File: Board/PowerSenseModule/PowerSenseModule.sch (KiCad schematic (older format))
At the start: 24 parts, among them J1 Conn_01x06_Male, U1 TPS82150

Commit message: Cleaned up main page of the schematic
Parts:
- added F?: Fuse, symbol Device:Fuse
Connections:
- net labels added: CANH, CANL, LIVE_IN, MEAS_IN, MEAS_OUT
- wire segments 101 -> 96
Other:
- note added: "MEAS_IN needs to be physically placed after caps\n"
- moved on the sheet: C1, C19, C2, C20, C21, C22, C23, C3, C4, C5, C6, C7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

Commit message: PCB update
- Laid out buck converter
- Laid out TE connector, TVS diode, and power sense resistor
- Created footprint for 4-pin crystal
- Updated crystal symbol
- Fixed design rules
- Moses's PCB design file name appended with *_backup
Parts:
- removed F?: Fuse, symbol Device:Fuse
- C6: value 47uF -> 6.8uF; footprint Capacitor_SMD:CP_Elec_4x5.8 -> Capacitor_SMD:C_0805_2012Metric_Pad1.15x1.40mm_HandSolder; symbol Device:CP -> Device:C
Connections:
- wire segments 96 -> 95
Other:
- note added: "Approximately 50% duty cycle \nat 50KHz from PWM module\n"
- moved on the sheet: D1
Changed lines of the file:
@@
 Wire Wire Line
 	2950 1300 3400 1300
-Connection ~ 2950 1300
 Wire Wire Line
 	2950 1550 2950 1300
@@
 $EndComp
 $Comp
-L Device:CP C6
+L Device:C C6
 U 1 1 5D3208C5
 P 5250 1700
 F 0 "C6" H 5365 1746 50  0000 L CNN
-F 1 "47uF" H 5365 1655 50  0000 L CNN
-F 2 "Capacitor_SMD:CP_Elec_4x5.8" H 5288 1550 50  0001 C CNN
+F 1 "6.8uF" H 5365 1655 50  0000 L CNN
+F 2 "Capacitor_SMD:C_0805_2012Metric_Pad1.15x1.40mm_HandSolder" H 5288 1550 50  0001 C CNN
 F 3 "~" H 5250 1700 50  0001 C CNN
 	1    5250 1700
@@
 	1    0    0    -1
 $EndComp
-Wire Wire Line
-	1800 1300 2175 1300
 $Comp
 L Device:D_Zener D1
 U 1 1 5DEFEB23
-P 2175 1550
-F 0 "D1" V 2129 1629 50  0000 L CNN
-F 1 "SD05-7" V 2220 1629 50  0000 L CNN
-F 2 "Diode_SMD:D_SOD-323_HandSoldering" H 2175 1550 50  0001 C CNN
-F 3 "https://www.mouser.com/ProductDetail/Diodes-Incorporated/SD05-7?qs=%2Fha2pyFadugD%2Fr1MYEydUCcSjftG2Vlq5z2%2Fe2tdzfA%3D" H 2175 1550 50  0001 C CNN
-	1    2175 1550
+P 2375 1550
+F 0 "D1" V 2329 1629 50  0000 L CNN
+F 1 "SD05-7" V 2420 1629 50  0000 L CNN
+F 2 "Diode_SMD:D_SOD-323_HandSoldering" H 2375 1550 50  0001 C CNN
+F 3 "https://www.mouser.com/ProductDetail/Diodes-Incorporated/SD05-7?qs=%2Fha2pyFadugD%2Fr1MYEydUCcSjftG2Vlq5z2%2Fe2tdzfA%3D" H 2375 1550 50  0001 C CNN
+	1    2375 1550
 	0    1    1    0
 $EndComp
 Wire Wire Line
-	2175 1400 2175 1300
-Connection ~ 2175 1300
+	2375 1400 2375 1300
 $Comp
 L power:GND #PWR02
 U 1 1 5DF00A75
-P 2175 1775
-F 0 "#PWR02" H 2175 1525 50  0001 C CNN
-F 1 "GND" H 2180 1602 50  0000 C CNN
-F 2 "" H 2175 1775 50  0001 C CNN
-F 3 "" H 2175 1775 50  0001 C CNN
-	1    2175 1775
-	1    0    0    -1
-$EndComp
-Wire Wire Line
-	2175 1775 2175 1700
+P 2375 1775
+F 0 "#PWR02" H 2375 1525 50  0001 C CNN
+F 1 "GND" H 2380 1602 50  0000 C CNN
+F 2 "" H 2375 1775 50  0001 C CNN
+F 3 "" H 2375 1775 50  0001 C CNN
+	1    2375 1775
+	1    0    0    -1
+$EndComp
+Wire Wire Line
+	2375 1775 2375 1700
 $Comp
 L Device:D D2
@@
 Text Notes 10000 4525 0    50   ~ 0
 35 to 50V cap and diode \nrating\n
-Wire Wire Line
-	2175 1300 2950 1300
-$Comp
-L Device:Fuse F?
-U 1 1 5DFE1622
-P 1650 1300
-F 0 "F?" V 1453 1300 50  0000 C CNN
-F 1 "Fuse" V 1544 1300 50  0000 C CNN
-F 2 "" V 1580 1300 50  0001 C CNN
-F 3 "~" H 1650 1300 50  0001 C CNN
-	1    1650 1300
-	0    1    1    0
-$EndComp
 Text Label 3900 3400 2    50   ~ 0
 MEAS_IN
@@
 Wire Wire Line
 	3900 4075 4025 4075
-Text Label 1375 1300 2    50   ~ 0
+Text Label 2250 1300 2    50   ~ 0
 LIVE_IN
-Wire Wire Line
-	1375 1300 1500 1300
 Text Label 2025 3400 0    50   ~ 0
 LIVE_IN
@@
 Text Notes 675  6325 0    50   ~ 0
 MEAS_IN needs to be physically placed after caps\n
+Text Notes 9925 4775 0    50   ~ 0
+Approximately 50% duty cycle \nat 50KHz from PWM module\n
+Wire Wire Line
+	2250 1300 2375 1300
+Wire Wire Line
+	2950 1300 2375 1300
+Connection ~ 2950 1300
+Connection ~ 2375 1300
 $EndSCHEMATC

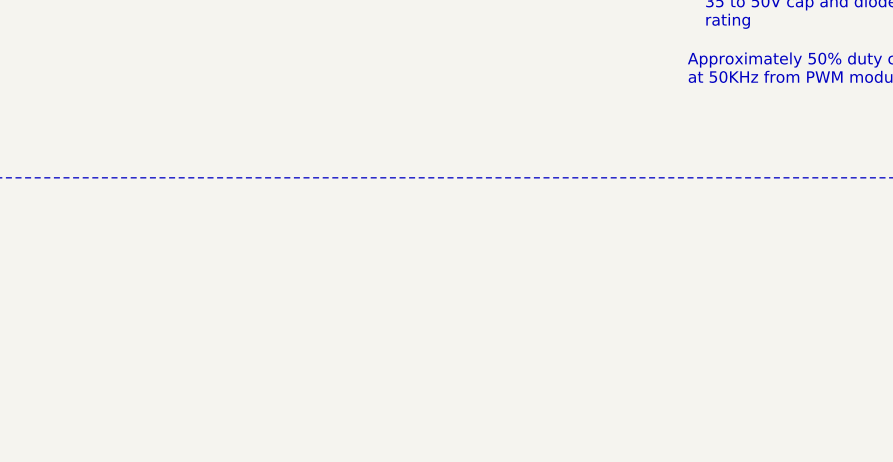
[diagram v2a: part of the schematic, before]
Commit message: Changed crystal gnd net and working on layout
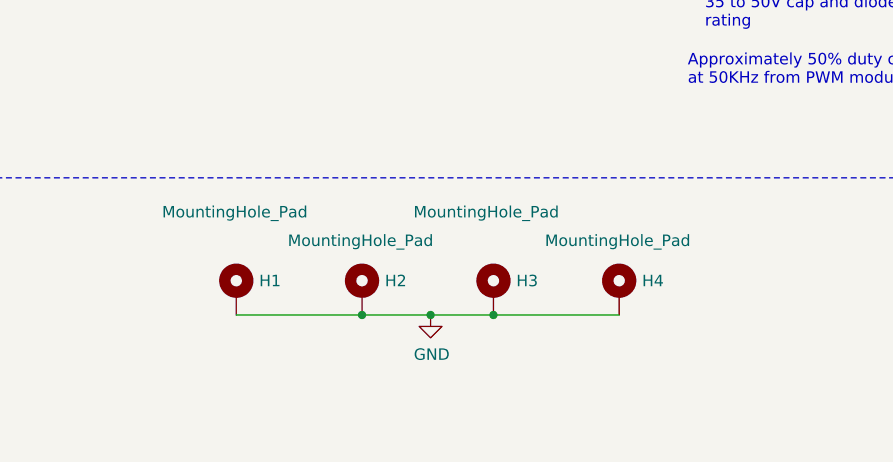
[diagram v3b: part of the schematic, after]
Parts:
- added H1, H2, H3, H4: MountingHole_Pad, MountingHole:MountingHole_2.7mm_M2.5_Pad, symbol Mechanical:MountingHole_Pad
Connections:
- net GND: now also H1.1, H2.1, H3.1, H4.1
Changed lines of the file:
@@
 Connection ~ 2950 1300
 Connection ~ 2375 1300
+$Comp
+L Mechanical:MountingHole_Pad H4
+U 1 1 5DF32F9A
+P 9625 5675
+F 0 "H4" H 9725 5724 50  0000 L CNN
+F 1 "MountingHole_Pad" H 9300 5900 50  0000 L CNN
+F 2 "MountingHole:MountingHole_2.7mm_M2.5_Pad" H 9625 5675 50  0001 C CNN
+F 3 "~" H 9625 5675 50  0001 C CNN
+	1    9625 5675
+	1    0    0    -1
+$EndComp
+$Comp
+L Mechanical:MountingHole_Pad H2
+U 1 1 5DF339FC
+P 8500 5675
+F 0 "H2" H 8600 5724 50  0000 L CNN
+F 1 "MountingHole_Pad" H 8175 5900 50  0000 L CNN
+F 2 "MountingHole:MountingHole_2.7mm_M2.5_Pad" H 8500 5675 50  0001 C CNN
+F 3 "~" H 8500 5675 50  0001 C CNN
+	1    8500 5675
+	1    0    0    -1
+$EndComp
+$Comp
+L Mechanical:MountingHole_Pad H3
+U 1 1 5DF34056
+P 9075 5675
+F 0 "H3" H 9175 5724 50  0000 L CNN
+F 1 "MountingHole_Pad" H 8725 6025 50  0000 L CNN
+F 2 "MountingHole:MountingHole_2.7mm_M2.5_Pad" H 9075 5675 50  0001 C CNN
+F 3 "~" H 9075 5675 50  0001 C CNN
+	1    9075 5675
+	1    0    0    -1
+$EndComp
+$Comp
+L Mechanical:MountingHole_Pad H1
+U 1 1 5DF3457C
+P 7950 5675
+F 0 "H1" H 8050 5724 50  0000 L CNN
+F 1 "MountingHole_Pad" H 7625 6025 50  0000 L CNN
+F 2 "MountingHole:MountingHole_2.7mm_M2.5_Pad" H 7950 5675 50  0001 C CNN
+F 3 "~" H 7950 5675 50  0001 C CNN
+	1    7950 5675
+	1    0    0    -1
+$EndComp
+Wire Wire Line
+	7950 5775 8500 5775
+Connection ~ 8500 5775
+Wire Wire Line
+	8500 5775 8800 5775
+Connection ~ 9075 5775
+Wire Wire Line
+	9075 5775 9625 5775
+$Comp
+L power:GND #PWR0108
+U 1 1 5DF4159C
+P 8800 5775
+F 0 "#PWR0108" H 8800 5525 50  0001 C CNN
+F 1 "GND" H 8805 5602 50  0000 C CNN
+F 2 "" H 8800 5775 50  0001 C CNN
+F 3 "" H 8800 5775 50  0001 C CNN
+	1    8800 5775
+	1    0    0    -1
+$EndComp
+Connection ~ 8800 5775
+Wire Wire Line
+	8800 5775 9075 5775
 $EndSCHEMATC

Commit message: layout 0.02
most power is routed
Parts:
- removed C20, C22: 0.1uF, Capacitor_SMD:C_0603_1608Metric, symbol Device:C
- added C? (x2): 0.1uF, Capacitor_SMD:C_0603_1608Metric, symbol Device:C
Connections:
- net GND: now also C23.2, C?.2, C?.2
- net GNDA: no longer C23.2
- net VS: now also C?.1
- net at D5.1 (K), D6.2 (A): now also C?.1
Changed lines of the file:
@@
-$EndComp
-$Comp
-L Device:C C20
-U 1 1 5E37E7E2
-P 8675 3725
-F 0 "C20" H 8790 3771 50  0000 L CNN
-F 1 "0.1uF" H 8790 3680 50  0000 L CNN
-F 2 "Capacitor_SMD:C_0603_1608Metric" H 8713 3575 50  0001 C CNN
-F 3 "~" H 8675 3725 50  0001 C CNN
-	1    8675 3725
-	1    0    0    -1
 $EndComp
 $Comp
@@
 Connection ~ 8100 3500
 Wire Wire Line
-	8675 3575 8675 3500
-Wire Wire Line
-	8675 3500 8500 3500
-Wire Wire Line
 	7675 3500 7575 3500
 Wire Wire Line
@@
 Wire Wire Line
 	8100 3875 8100 4225
-$Comp
-L power:GNDA #PWR022
-U 1 1 5E38CDB2
-P 8675 3900
-F 0 "#PWR022" H 8675 3650 50  0001 C CNN
-F 1 "GNDA" H 8680 3727 50  0000 C CNN
-F 2 "" H 8675 3900 50  0001 C CNN
-F 3 "" H 8675 3900 50  0001 C CNN
-	1    8675 3900
-	1    0    0    -1
-$EndComp
-Wire Wire Line
-	8675 3900 8675 3875
 $Comp
 L Device:D D6
@@
 $EndComp
 $Comp
-L Device:C C22
-U 1 1 5E394EC1
-P 9825 3725
-F 0 "C22" H 9940 3771 50  0000 L CNN
-F 1 "0.1uF" H 9940 3680 50  0000 L CNN
-F 2 "Capacitor_SMD:C_0603_1608Metric" H 9863 3575 50  0001 C CNN
-F 3 "~" H 9825 3725 50  0001 C CNN
-	1    9825 3725
-	1    0    0    -1
-$EndComp
-$Comp
 L Device:C C21
 U 1 1 5E394EC7
@@
 Connection ~ 9250 3500
 Wire Wire Line
-	9825 3575 9825 3500
-Wire Wire Line
-	9825 3500 9650 3500
-$Comp
-L power:GNDA #PWR027
-U 1 1 5E394ED5
-P 9825 3900
-F 0 "#PWR027" H 9825 3650 50  0001 C CNN
-F 1 "GNDA" H 9830 3727 50  0000 C CNN
-F 2 "" H 9825 3900 50  0001 C CNN
-F 3 "" H 9825 3900 50  0001 C CNN
-	1    9825 3900
-	1    0    0    -1
-$EndComp
-Wire Wire Line
-	9825 3900 9825 3875
-Wire Wire Line
-	8825 3500 8675 3500
-Connection ~ 8675 3500
-Wire Wire Line
 	9250 4225 8100 4225
 Wire Wire Line
@@
 Wire Wire Line
 	8100 4225 7575 4225
-Wire Wire Line
-	9825 3500 10325 3500
-Connection ~ 9825 3500
 $Comp
 L power:VS #PWR034
@@
 Wire Wire Line
 	5900 1300 6200 1300
-$Comp
-L Device:CP C23
-U 1 1 5E3BD7DC
-P 10325 3725
-F 0 "C23" H 10443 3771 50  0000 L CNN
-F 1 "4.7uF" H 10443 3680 50  0000 L CNN
-F 2 "Capacitor_SMD:CP_Elec_4x5.8" H 10363 3575 50  0001 C CNN
-F 3 "~" H 10325 3725 50  0001 C CNN
-	1    10325 3725
-	1    0    0    -1
-$EndComp
-Wire Wire Line
-	10325 3575 10325 3500
-Connection ~ 10325 3500
-Wire Wire Line
-	10325 3500 10450 3500
-$Comp
-L power:GNDA #PWR029
-U 1 1 5E3C0B37
-P 10325 3925
-F 0 "#PWR029" H 10325 3675 50  0001 C CNN
-F 1 "GNDA" H 10330 3752 50  0000 C CNN
-F 2 "" H 10325 3925 50  0001 C CNN
-F 3 "" H 10325 3925 50  0001 C CNN
-	1    10325 3925
-	1    0    0    -1
-$EndComp
-Wire Wire Line
-	10325 3925 10325 3875
 Text Label 7575 4225 2    50   ~ 0
 PWM
@@
 Wire Wire Line
 	8800 5775 9075 5775
+$Comp
+L power:GND #PWR?
+U 1 1 5E0590E1
+P 8680 3870
+F 0 "#PWR?" H 8680 3620 50  0001 C CNN
+F 1 "GND" H 8685 3697 50  0000 C CNN
+F 2 "" H 8680 3870 50  0001 C CNN
+F 3 "" H 8680 3870 50  0001 C CNN
+	1    8680 3870
+	1    0    0    -1
+$EndComp
+$Comp
+L Device:C C?
+U 1 1 5E0635BE
+P 8680 3720
+F 0 "C?" H 8795 3766 50  0000 L CNN
+F 1 "0.1uF" H 8795 3675 50  0000 L CNN
+F 2 "Capacitor_SMD:C_0603_1608Metric" H 8718 3570 50  0001 C CNN
+F 3 "~" H 8680 3720 50  0001 C CNN
+	1    8680 3720
+	1    0    0    -1
+$EndComp
+Wire Wire Line
+	8500 3500 8680 3500
+Wire Wire Line
+	8680 3570 8680 3500
+Connection ~ 8680 3500
+Wire Wire Line
+	8680 3500 8825 3500
+$Comp
+L power:GND #PWR?
+U 1 1 5E06D28B
+P 9880 3920
+F 0 "#PWR?" H 9880 3670 50  0001 C CNN
+F 1 "GND" H 9885 3747 50  0000 C CNN
+F 2 "" H 9880 3920 50  0001 C CNN
+F 3 "" H 9880 3920 50  0001 C CNN
+	1    9880 3920
+	1    0    0    -1
+$EndComp
+Wire Wire Line
+	9650 3500 9880 3500
+$Comp
+L Device:C C?
+U 1 1 5E07A737
+P 9880 3770
+F 0 "C?" H 9995 3816 50  0000 L CNN
+F 1 "0.1uF" H 9995 3725 50  0000 L CNN
+F 2 "Capacitor_SMD:C_0603_1608Metric" H 9918 3620 50  0001 C CNN
+F 3 "~" H 9880 3770 50  0001 C CNN
+	1    9880 3770
+	1    0    0    -1
+$EndComp
+Wire Wire Line
+	9880 3620 9880 3500
+Connection ~ 9880 3500
+$Comp
+L Device:CP C23
+U 1 1 5E3BD7DC
+P 10340 3720
+F 0 "C23" H 10458 3766 50  0000 L CNN
+F 1 "4.7uF" H 10458 3675 50  0000 L CNN
+F 2 "Capacitor_SMD:CP_Elec_4x5.8" H 10378 3570 50  0001 C CNN
+F 3 "~" H 10340 3720 50  0001 C CNN
+	1    10340 3720
+	1    0    0    -1
+$EndComp
+Wire Wire Line
+	9880 3500 10340 3500
+Wire Wire Line
+	10340 3570 10340 3500
+Connection ~ 10340 3500
+Wire Wire Line
+	10340 3500 10450 3500
+$Comp
+L power:GND #PWR?
+U 1 1 5E08E962
+P 10340 3870
+F 0 "#PWR?" H 10340 3620 50  0001 C CNN
+F 1 "GND" H 10345 3697 50  0000 C CNN
+F 2 "" H 10340 3870 50  0001 C CNN
+F 3 "" H 10340 3870 50  0001 C CNN
+	1    10340 3870
+	1    0    0    -1
+$EndComp
 $EndSCHEMATC

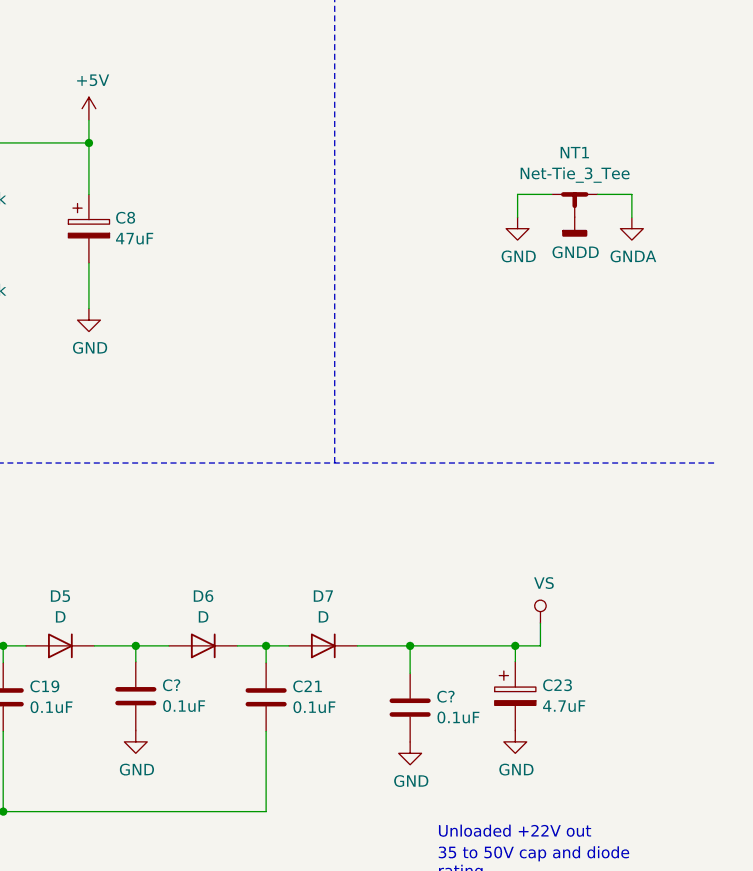
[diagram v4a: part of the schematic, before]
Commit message: layout 0.04
- Added top and bottom ground plane
- changed GNDD to GND
- readjusted spacing between components
- made the board a little smaller
- fine tuned copper fills
- got pretty good power rail and ground layout
- length matched traces from sense resistor to op amp
- repositioned LEDs
- added text for LEDs

TODO:
- maybe reorganize passives between MCU and op amps
- layout/route the three resistors for the op amps currently on the bottom of the PCB
- move shunt resistor for CAN closer to connector (?)
- route length tuned traces for CANH and CANL
- GNDA copper fills
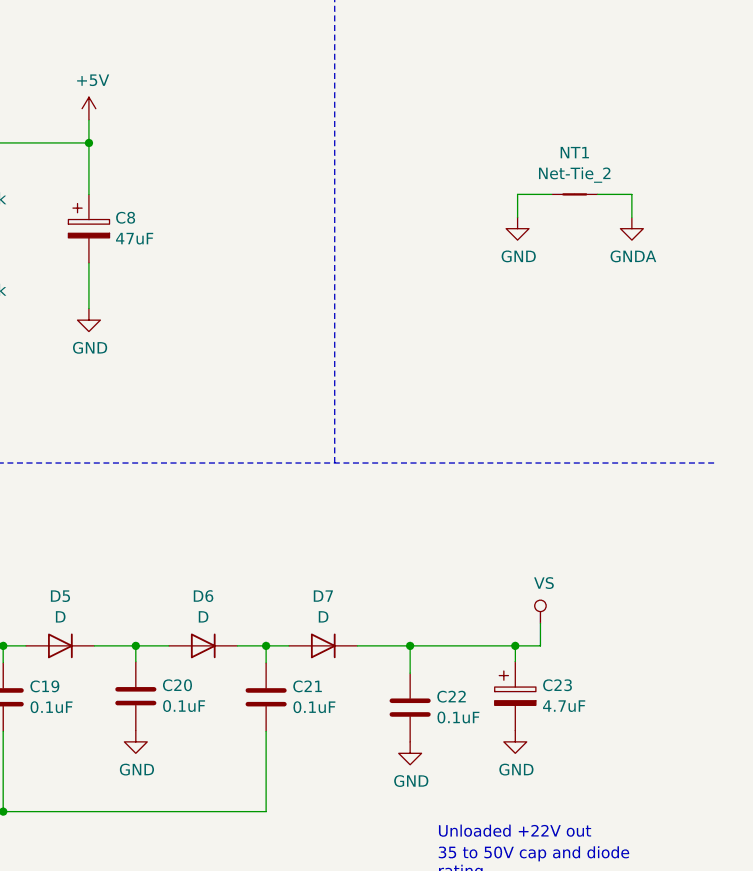
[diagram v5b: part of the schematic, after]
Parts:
- removed NT1: Net-Tie_3_Tee, NetTie:NetTie-3_SMD_Pad2.0mm, symbol Device:Net-Tie_3_Tee
- added NT1: Net-Tie_2, NetTie:NetTie-2_SMD_Pad2.0mm, symbol Device:Net-Tie_2
- gave numbers to parts that had none: 2
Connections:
- net GND: now also NT1.1
- net GNDA: now also NT1.2
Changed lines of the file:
@@
 Live_IN\n
-$Comp
-L power:GNDD #PWR013
-U 1 1 5D401FC5
-P 10600 1625
-F 0 "#PWR013" H 10600 1375 50  0001 C CNN
-F 1 "GNDD" H 10604 1470 50  0000 C CNN
-F 2 "" H 10600 1625 50  0001 C CNN
-F 3 "" H 10600 1625 50  0001 C CNN
-	1    10600 1625
-	1    0    0    -1
-$EndComp
 $Comp
 L power:GNDA #PWR014
@@
 F 3 "~" H 2950 1700 50  0001 C CNN
 	1    2950 1700
-	1    0    0    -1
-$EndComp
-$Comp
-L Device:Net-Tie_3_Tee NT1
-U 1 1 5D4008D3
-P 10600 1525
-F 0 "NT1" H 10600 1706 50  0000 C CNN
-F 1 "Net-Tie_3_Tee" H 10600 1615 50  0000 C CNN
-F 2 "NetTie:NetTie-3_SMD_Pad2.0mm" H 10600 1525 50  0001 C CNN
-F 3 "~" H 10600 1525 50  0001 C CNN
-	1    10600 1525
 	1    0    0    -1
 $EndComp
@@
 	8800 5775 9075 5775
 $Comp
-L power:GND #PWR?
+L power:GND #PWR013
 U 1 1 5E0590E1
 P 8680 3870
-F 0 "#PWR?" H 8680 3620 50  0001 C CNN
+F 0 "#PWR013" H 8680 3620 50  0001 C CNN
 F 1 "GND" H 8685 3697 50  0000 C CNN
 F 2 "" H 8680 3870 50  0001 C CNN
@@
 $EndComp
 $Comp
-L Device:C C?
+L Device:C C20
 U 1 1 5E0635BE
 P 8680 3720
-F 0 "C?" H 8795 3766 50  0000 L CNN
+F 0 "C20" H 8795 3766 50  0000 L CNN
 F 1 "0.1uF" H 8795 3675 50  0000 L CNN
 F 2 "Capacitor_SMD:C_0603_1608Metric" H 8718 3570 50  0001 C CNN
@@
 	8680 3500 8825 3500
 $Comp
-L power:GND #PWR?
+L power:GND #PWR016
 U 1 1 5E06D28B
 P 9880 3920
-F 0 "#PWR?" H 9880 3670 50  0001 C CNN
+F 0 "#PWR016" H 9880 3670 50  0001 C CNN
 F 1 "GND" H 9885 3747 50  0000 C CNN
 F 2 "" H 9880 3920 50  0001 C CNN
@@
 	9650 3500 9880 3500
 $Comp
-L Device:C C?
+L Device:C C22
 U 1 1 5E07A737
 P 9880 3770
-F 0 "C?" H 9995 3816 50  0000 L CNN
+F 0 "C22" H 9995 3816 50  0000 L CNN
 F 1 "0.1uF" H 9995 3725 50  0000 L CNN
 F 2 "Capacitor_SMD:C_0603_1608Metric" H 9918 3620 50  0001 C CNN
@@
 	10340 3500 10450 3500
 $Comp
-L power:GND #PWR?
+L power:GND #PWR018
 U 1 1 5E08E962
 P 10340 3870
-F 0 "#PWR?" H 10340 3620 50  0001 C CNN
+F 0 "#PWR018" H 10340 3620 50  0001 C CNN
 F 1 "GND" H 10345 3697 50  0000 C CNN
 F 2 "" H 10340 3870 50  0001 C CNN
@@
 	1    0    0    -1
 $EndComp
+$Comp
+L Device:Net-Tie_2 NT1
+U 1 1 5DF596E6
+P 10600 1525
+F 0 "NT1" H 10600 1706 50  0000 C CNN
+F 1 "Net-Tie_2" H 10600 1615 50  0000 C CNN
+F 2 "NetTie:NetTie-2_SMD_Pad2.0mm" H 10600 1525 50  0001 C CNN
+F 3 "~" H 10600 1525 50  0001 C CNN
+	1    10600 1525
+	1    0    0    -1
+$EndComp

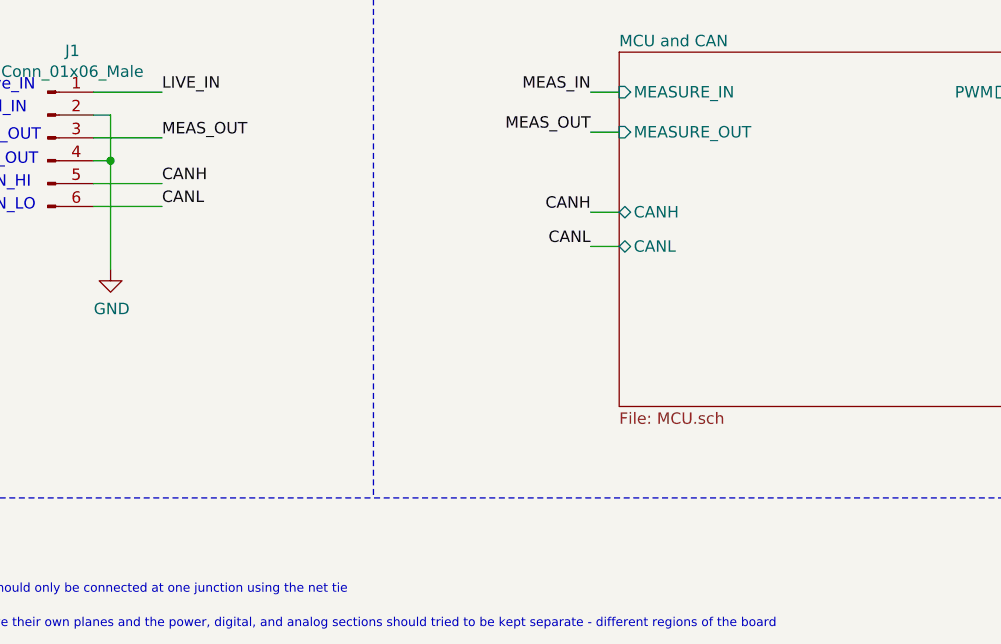
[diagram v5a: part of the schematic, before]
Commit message: layout 0.05
- differential pair for CAN bus
- differential pair for shunt resistor
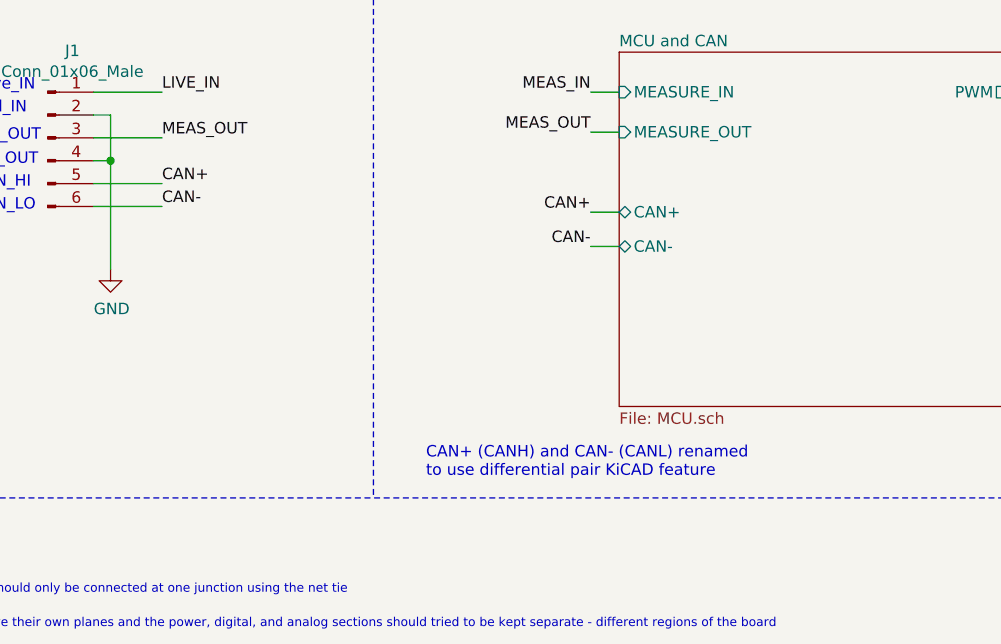
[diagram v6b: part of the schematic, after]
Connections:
- net CANH renamed CAN+
- net CANL renamed CAN-
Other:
- note added: "CAN+ (CANH) and CAN- (CANL) renamed \nto use differential pair KiCAD feature"
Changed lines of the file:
@@
 F0 "MCU and CAN" 50
 F1 "MCU.sch" 50
-F2 "CANH" T L 4025 3925 50
-F3 "CANL" T L 4025 4075 50
+F2 "CAN+" T L 4025 3925 50
+F3 "CAN-" T L 4025 4075 50
 F4 "MEASURE_IN" I L 4025 3400 50
 F5 "MEASURE_OUT" I L 4025 3575 50
@@
 	3900 3575 4025 3575
 Text Label 3900 3925 2    50   ~ 0
-CANH
+CAN+
 Wire Wire Line
 	3900 3925 4025 3925
 Text Label 3900 4075 2    50   ~ 0
-CANL
+CAN-
 Wire Wire Line
 	3900 4075 4025 4075
@@
 MEAS_OUT
 Text Label 2025 3800 0    50   ~ 0
-CANH
+CAN+
 Text Label 2025 3900 0    50   ~ 0
-CANL
+CAN-
 Text Label 5425 1300 0    50   ~ 0
 MEAS_IN
@@
 	1    0    0    -1
 $EndComp
+Text Notes 3180 5090 0    50   ~ 0
+CAN+ (CANH) and CAN- (CANL) renamed \nto use differential pair KiCAD feature
 $EndSCHEMATC
